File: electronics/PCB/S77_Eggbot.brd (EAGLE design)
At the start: 95.2 x 68.2 mm, 5 parts, among them U1 CR_LM2596, U2 S2_MINI, U3 CARRIER_A4988, U4 CARRIER_A4988, X1 POLLIN_JACK_A

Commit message: WIP: fix board dimension and place components
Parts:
- added C1, C2: 100µF/35V/0R056, rcl:E3,5-8
- added D1: 1N5822, lib_s77_eggbot:DO201T15
- added JP1, JP2, JP3: (no value), pinhead:1X04
- added JP4: (no value), pinhead:1X08
- added SERVO: (no value), pinhead:1X03
- added SJ1, SJ2, SJ3, SJ4, SJ5, SJ6: (no value), jumper:SJ
- added X2, X3: B6B-PH, lib_s77_eggbot:B6B-PH
- X1: value POLLIN_JACK_A -> PWR
- moved U1 90.0 mm to (1.00, 36.0), turned to 0 degrees
- moved U2 28.1 mm to (0.00, 35.0), turned to 270 degrees
- moved X1 14.3 mm to (10.5, 47.0), turned to 270 degrees
- moved U4 6.40 mm to (52.5, 45.0)
- moved U3 5.94 mm to (52.5, 20.0)
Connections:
- new net +5V: JP1.2, U1.4
- new net N$10: JP3.4, U4.14, X3.6
- new net N$11: SJ1.2, U3.2
- new net N$12: SJ2.2, U3.3
- new net N$13: SJ3.2, U3.4
- new net N$14: U3.1
- new net N$15: U3.8
- new net N$16: U3.7
- new net N$17: SJ4.2, U4.2
- new net N$18: SJ5.2, U4.3
- new net N$19: SJ6.2, U4.4
- new net N$2: JP2.1, U3.11, X2.1
- new net N$3: D1.A, X1.1
- new net N$4: JP2.2, U3.12, X2.2
- new net N$5: JP2.3, U3.13, X2.4
- new net N$6: JP2.4, U3.14, X2.6
- new net N$7: JP3.1, U4.11, X3.1
- new net N$8: JP3.2, U4.12, X3.2
- new net N$9: JP3.3, U4.13, X3.4
- net +3V3: now also JP1.3, SJ1.1, SJ2.1, SJ3.1, SJ4.1, SJ5.1, SJ6.1, U3.10, U3.5, U3.6, U4.5, U4.6
- net GND: now also C1.-, C2.-, JP1.4, X1.2
- net VDD: no longer U3.10
- net VMOT: now also C1.+, C2.+, D1.C, JP1.1, U1.1
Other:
- board size 95.2 x 68.2 mm -> 70 x 70 mm
- board text added: "GND +5V PWM"

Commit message: first version of schematic and layout
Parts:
- JP4: device pinhead:1X08 -> pinhead:1X12
- moved JP4 2.24 mm to (29.0, 4.50)
- moved JP2 1.12 mm to (62.5, 19.0)
- moved JP3 1.12 mm to (62.5, 44.0)
- moved SJ5 1.00 mm to (42.5, 49.0)
- moved SJ6 1.00 mm to (42.5, 46.0)
- moved SJ4 0.50 mm to (42.5, 52.0)
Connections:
- removed net N$1: U1.2, U1.3
- removed net N$14: U3.1
- removed net N$15: U3.8
- removed net N$16: U3.7
- removed net VBUS: U2.9
- removed net VDD: U4.10
- new net DIR1: U2.18, U3.8
- new net DIR2: U2.19, U4.8
- new net N$20: JP4.4, U2.4
- new net N$21: JP4.3, U2.5
- new net N$22: JP4.2, U2.6
- new net N$23: JP4.5, U2.27
- new net N$24: JP4.6, U2.12
- new net N$25: JP4.7, U2.13
- new net N$26: JP4.9, U2.29
- new net N$27: JP4.8, U2.14
- new net N$28: JP4.11, U2.30
- new net N$29: JP4.10, U2.15
- new net SERVO_PWM: SERVO.3, U2.20
- new net STEP1: U2.2, U3.7
- new net STEP2: U2.3, U4.7
- new net STEPPER_EN: U2.17, U3.1, U4.1
- net +3V3: now also JP4.1, U4.10
- net +5V: now also SERVO.2, U2.9
- net GND: now also JP4.12, SERVO.1, U1.2, U1.3
- net N$4: now also X2.3; no longer X2.2
- net N$8: now also X3.3; no longer X3.2
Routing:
- net +3V3: track 0.00 -> 191.0 mm, vias 0 -> 1
- net +5V: track 0.00 -> 141.7 mm
- net VMOT: track 0.00 -> 124.1 mm
- net STEPPER_EN: track 0.00 -> 47.6 mm
- net SERVO_PWM: track 0.00 -> 47.4 mm
- net DIR2: track 0.00 -> 32.3 mm
- net N$21: track 0.00 -> 31.8 mm
- net N$20: track 0.00 -> 31.8 mm
- net N$22: track 0.00 -> 31.8 mm
- net DIR1: track 0.00 -> 31.5 mm
- net STEP1: track 0.00 -> 31.2 mm
- net STEP2: track 0.00 -> 31.2 mm
- net N$26: track 0.00 -> 25.3 mm
- net N$28: track 0.00 -> 25.3 mm
- net N$23: track 0.00 -> 17.3 mm
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- added copper zone on layer 1, net GND
- added copper zone on layer 16, net GND
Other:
- board text added: "+3V3"
- board text added: "+5V"
- board text added: "11"
- board text added: "17"
- board text added: "18"
- board text added: "33"
- board text added: "34"
- board text added: "35"
- board text added: "36"
- board text added: "37"
- board text added: "3V3"
- board text added: "7"
- board text added: "9"
- board text added: "GND"
- board text added: "MS1"
- board text added: "MS2"
- board text added: "MS3"
- board text added: "PWM +5V GND"
- board text added: "VMOT"
- board text removed: "GND +5V PWM"

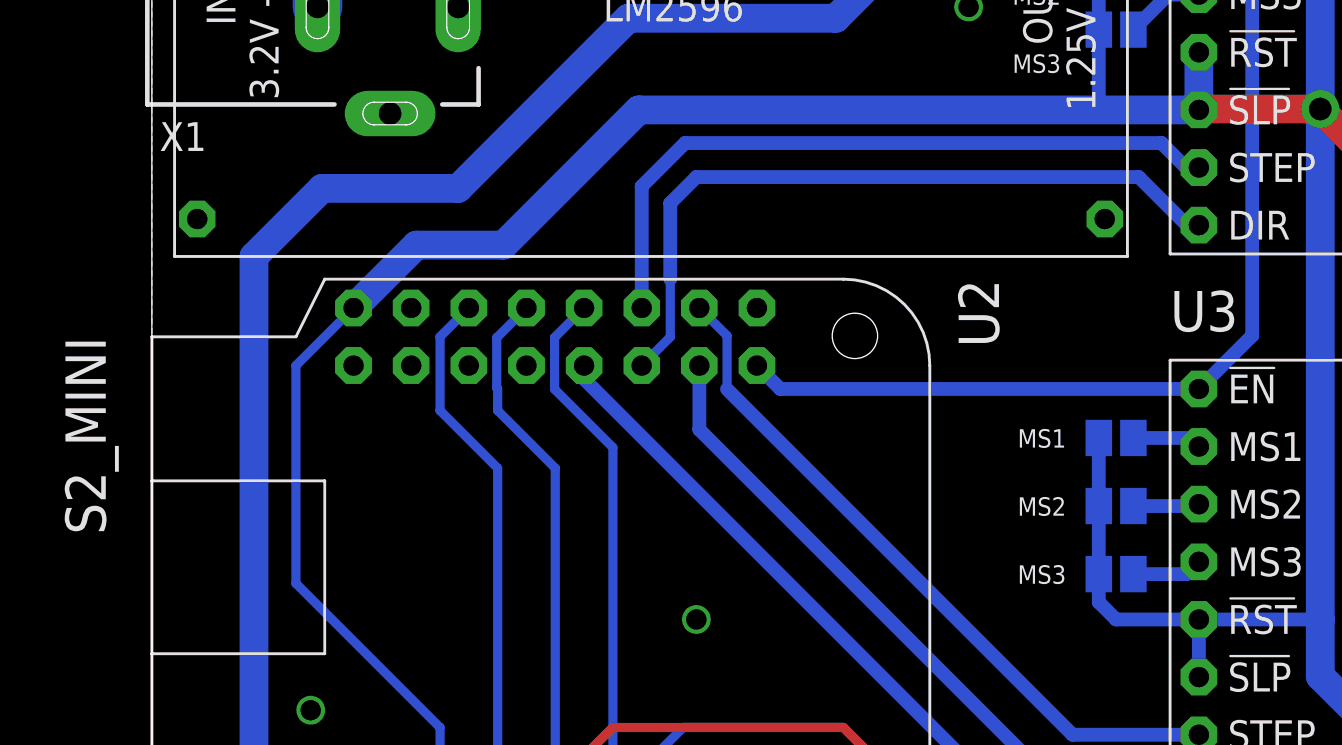
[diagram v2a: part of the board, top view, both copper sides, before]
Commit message: PCB: fix smaller details, update docs
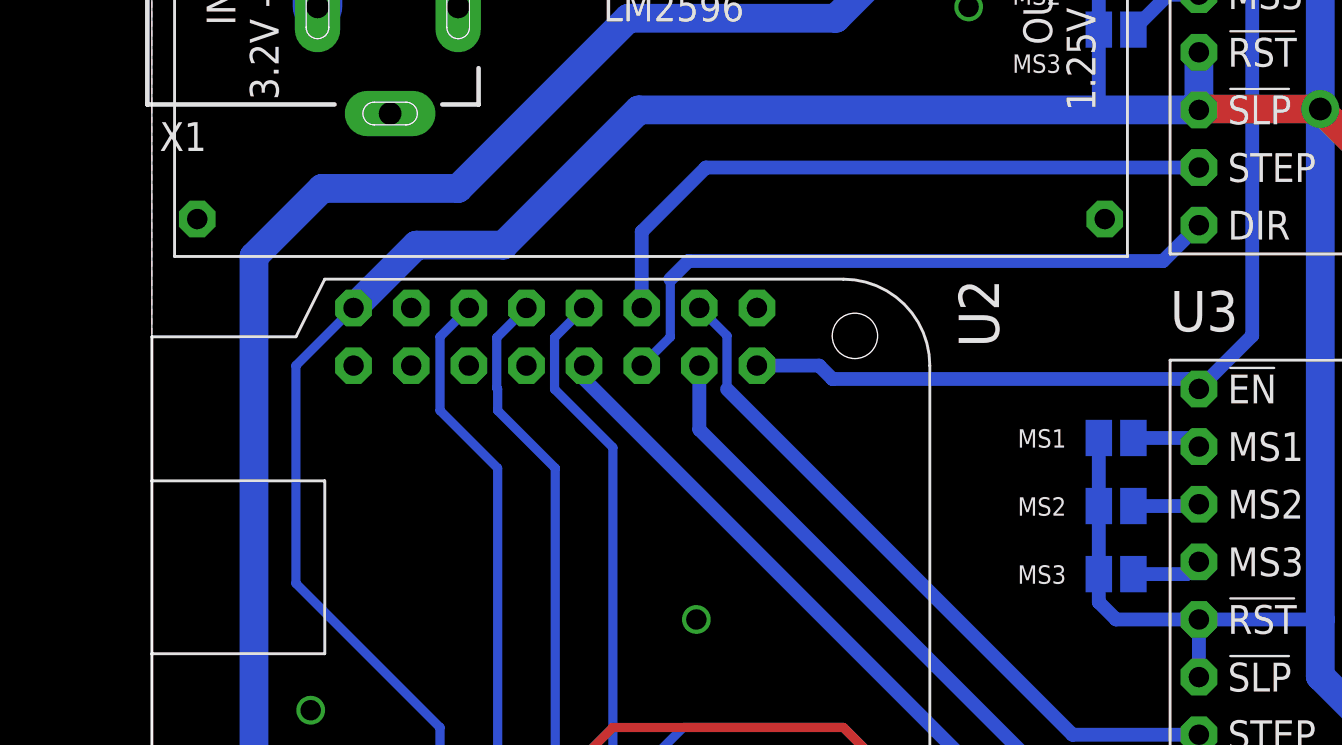
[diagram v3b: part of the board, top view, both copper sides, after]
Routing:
- net DIR2: track 32.3 -> 28.6 mm
- net STEP2: track 31.2 -> 29.1 mm
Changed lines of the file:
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@@
 <setting verticaltext="up"/>
 </settings>
-<grid distance="1" unitdist="mm" unit="mm" style="lines" multiple="1" display="no" altdistance="0.025" altunitdist="inch" altunit="inch"/>
+<grid distance="0.2" unitdist="mm" unit="mm" style="lines" multiple="1" display="no" altdistance="0.025" altunitdist="inch" altunit="inch"/>
 <layers>
 <layer number="1" name="Top" color="4" fill="1" visible="yes" active="yes"/>
@@
 <attribute name="NAME" x="44.88" y="32.7" size="1.778" layer="25"/>
 </element>
-<element name="U2" library="lib_s77_eggbot" package="S2_MINI" value="S2_MINI" x="0" y="35" rot="R270"/>
+<element name="U2" library="lib_s77_eggbot" package="S2_MINI" value="S2_MINI" x="0" y="35" smashed="yes" rot="R270">
+<attribute name="NAME" x="35.56" y="35" size="1.778" layer="25" rot="R270"/>
+</element>
 <element name="U1" library="lib_s77_eggbot" package="CR_LM2596" value="CR_LM2596" x="1" y="36" smashed="yes">
 <attribute name="NAME" x="1" y="57.59" size="1.778" layer="25"/>
@@
 <element name="X3" library="lib_s77_eggbot" package="B6B-PH" value="B6B-PH" x="67" y="43" smashed="yes" rot="R90">
 <attribute name="NAME" x="67" y="34.25" size="1.27" layer="25"/>
-<attribute name="VALUE" x="71.5" y="36.25" size="1.27" layer="27" rot="R90"/>
 </element>
 <element name="JP3" library="pinhead" package="1X04" value="" x="62.5" y="44" rot="R90"/>
@@
 <contactref element="U3" pad="1"/>
 <contactref element="U4" pad="1"/>
-<wire x1="46.15" y1="30.16" x2="27.7" y2="30.16" width="0.6096" layer="16"/>
-<wire x1="27.7" y1="30.16" x2="26.67" y2="31.19" width="0.6096" layer="16"/>
 <wire x1="46.15" y1="55.16" x2="47.34" y2="55.16" width="0.6096" layer="16"/>
 <wire x1="47.34" y1="55.16" x2="48.5" y2="54" width="0.6096" layer="16"/>
 <wire x1="48.5" y1="54" x2="48.5" y2="32.51" width="0.6096" layer="16"/>
 <wire x1="48.5" y1="32.51" x2="46.15" y2="30.16" width="0.6096" layer="16"/>
+<wire x1="26.67" y1="31.19" x2="29.41" y2="31.19" width="0.6096" layer="16"/>
+<wire x1="29.41" y1="31.19" x2="30" y2="30.6" width="0.6096" layer="16"/>
+<wire x1="30" y1="30.6" x2="45.71" y2="30.6" width="0.6096" layer="16"/>
+<wire x1="45.71" y1="30.6" x2="46.15" y2="30.16" width="0.6096" layer="16"/>
 </signal>
 <signal name="DIR1">
@@
 <contactref element="U2" pad="19"/>
 <contactref element="U4" pad="8"/>
-<wire x1="46.15" y1="37.38" x2="45.62" y2="37.38" width="0.6096" layer="16"/>
-<wire x1="45.62" y1="37.38" x2="43.5" y2="39.5" width="0.6096" layer="16"/>
-<wire x1="43.5" y1="39.5" x2="24" y2="39.5" width="0.6096" layer="16"/>
-<wire x1="24" y1="39.5" x2="22.85" y2="38.35" width="0.6096" layer="16"/>
 <wire x1="21.59" y1="31.19" x2="22.85" y2="32.45" width="0.4064" layer="16"/>
 <wire x1="22.85" y1="32.45" x2="22.85" y2="35" width="0.4064" layer="16"/>
-<wire x1="22.85" y1="35" x2="22.85" y2="38.35" width="0.6096" layer="16"/>
+<wire x1="46.15" y1="37.38" x2="44.57" y2="35.8" width="0.6096" layer="16"/>
+<wire x1="44.57" y1="35.8" x2="23.65" y2="35.8" width="0.6096" layer="16"/>
+<wire x1="23.65" y1="35.8" x2="22.85" y2="35" width="0.6096" layer="16"/>
 </signal>
 <signal name="STEP2">
 <contactref element="U2" pad="3"/>
 <contactref element="U4" pad="7"/>
-<wire x1="46.15" y1="39.92" x2="45.58" y2="39.92" width="0.6096" layer="16"/>
-<wire x1="45.58" y1="39.92" x2="44.5" y2="41" width="0.6096" layer="16"/>
-<wire x1="44.5" y1="41" x2="23.5" y2="41" width="0.6096" layer="16"/>
-<wire x1="23.5" y1="41" x2="21.59" y2="39.09" width="0.6096" layer="16"/>
-<wire x1="21.59" y1="33.73" x2="21.59" y2="39.09" width="0.6096" layer="16"/>
+<wire x1="21.59" y1="33.73" x2="21.59" y2="37.09" width="0.6096" layer="16"/>
+<wire x1="46.15" y1="39.92" x2="24.42" y2="39.92" width="0.6096" layer="16"/>
+<wire x1="24.42" y1="39.92" x2="21.59" y2="37.09" width="0.6096" layer="16"/>
 </signal>
 <signal name="SERVO_PWM">

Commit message: Add QR Code to board layout, export gerber files
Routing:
- net VMOT: track 124.1 -> 125.0 mm
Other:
- board text added: "ATTENTION: Trim output to 5V before installing U2, U3 and U4"
- board text added: "S77 EggBot 25.01.2024"
